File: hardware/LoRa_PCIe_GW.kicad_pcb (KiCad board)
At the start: 6 copper layers, 50.9 x 30 mm, 247 parts, among them Q600 NC, U100 SX1303, U201 3V3, U202 TPS62242DRV, U203 3V3, U204 STTS751, U205 NCP176BMX330TCG, U206 3V3, U300 RP2040, U301 GD25Q16EEIGR, U600 ZOE-M8Q, U700 NC, U800 SX1250, U801 SAW Filter, U802 SKY66423-11, U803 SAW Filter, U805 SAW Filter, U900 SX1250, Y300 12 MHz, Y800 TCXO

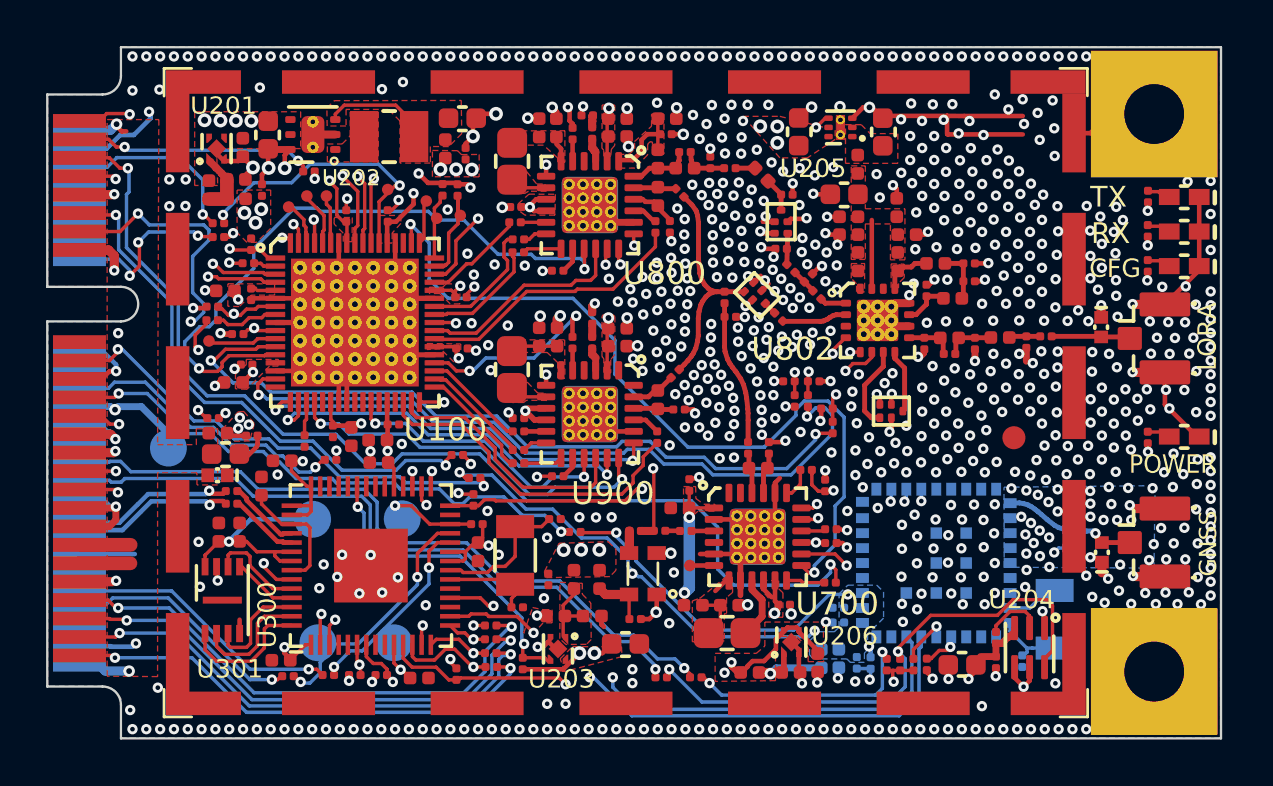
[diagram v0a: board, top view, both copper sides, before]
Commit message: Fixed couple of IO position issues. Controlled everything again.
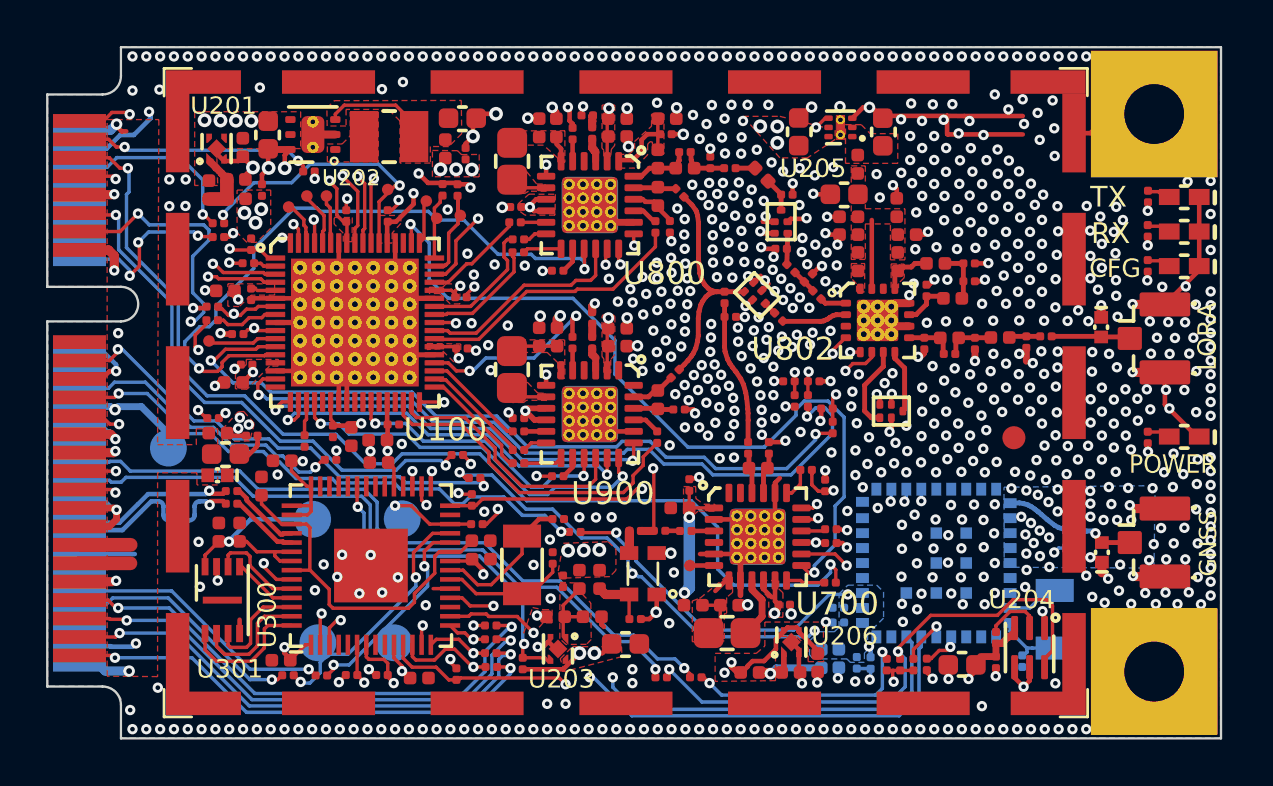
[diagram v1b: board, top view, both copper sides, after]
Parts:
- added C1: 0.1uF, LoRa_PCIe_GW:rlc_402_smd_small, F.Cu at (118.8, 121.4)
- moved C303 2.64 mm to (121.9, 122.2), turned to 90 degrees
- moved C208 0.64 mm to (122.4, 123.2)
- moved Y300 0.51 mm to (120.6, 122.5)
- moved C6 0.35 mm to (118.8, 122.2), turned to 0 degrees
- moved R322 0.30 mm to (111.9, 127.3)
- moved FB205 0.24 mm to (123.1, 123.1)
- moved C304 0.14 mm to (122.2, 120.5)
- moved R333 0.14 mm to (113.2, 127.2)
- moved R312 0.07 mm to (118.4, 119.7)
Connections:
- C8 pad 1: Net-(C8-Pad1) -> Net-(U300-Pad23)
- U300 pad 19: unconnected-(U300-Pad19) -> GND
- U300 pad 2: I2C_SCL -> I2C_SDA
- U300 pad 23: VCCIO33 -> Net-(U300-Pad23)
- U300 pad 3: I2C_SDA -> I2C_SCL
- U300 pad 45: Net-(C8-Pad1) -> Net-(U300-Pad23)
- U300 pad 50: Net-(C8-Pad1) -> Net-(U300-Pad23)
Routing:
- net Net-(U300-Pad23): track 0.00 -> 15.5 mm
- net Net-(C8-Pad1): track 5.42 -> 0.00 mm
- net /SCH2/USB_D+: track 7.03 -> 9.47 mm
- net Net-(C303-Pad1): track 3.98 -> 5.46 mm
- net I2C_SCL: track 48.6 -> 47.5 mm
- net VCCIO33: track 42.3 -> 41.4 mm, vias 17 -> 18
- net I2C_SDA: track 50.0 -> 50.8 mm
- net HOST_UART_TX: track 31.1 -> 30.3 mm
- net HOST_MOSI: track 53.9 -> 53.1 mm
- net GND: track 134.5 -> 135.2 mm
- net /SCH2/H_UART_TX: track 17.9 -> 18.6 mm
- net /SCH2/DBG_SWDIO: track 10.9 -> 11.5 mm

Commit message: Fixed ERC and Schematic to Layout parity errors.
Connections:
- U205 pad 5: (no net) -> unconnected-(U205-Pad5)
- U301 pad 9: (no net) -> unconnected-(U301-Pad9)
- U600 pad 10: (no net) -> unconnected-(U600-Pad10)
- U600 pad 11: (no net) -> unconnected-(U600-Pad11)
- U600 pad 17: (no net) -> unconnected-(U600-Pad17)
- U600 pad 28: (no net) -> unconnected-(U600-Pad28)
- U600 pad 3: (no net) -> unconnected-(U600-Pad3)
- U600 pad 36: (no net) -> unconnected-(U600-Pad36)
- U600 pad 4: (no net) -> unconnected-(U600-Pad4)
